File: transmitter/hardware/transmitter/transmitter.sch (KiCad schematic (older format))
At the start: 29 parts, among them J1 SOIL, J2 SOIL, J3 USB_UART, J4 PWR, J5 SOIL, J6 SOIL, J7 SOIL, J8 SOIL, SW1 SW_SPST, SW2 SW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

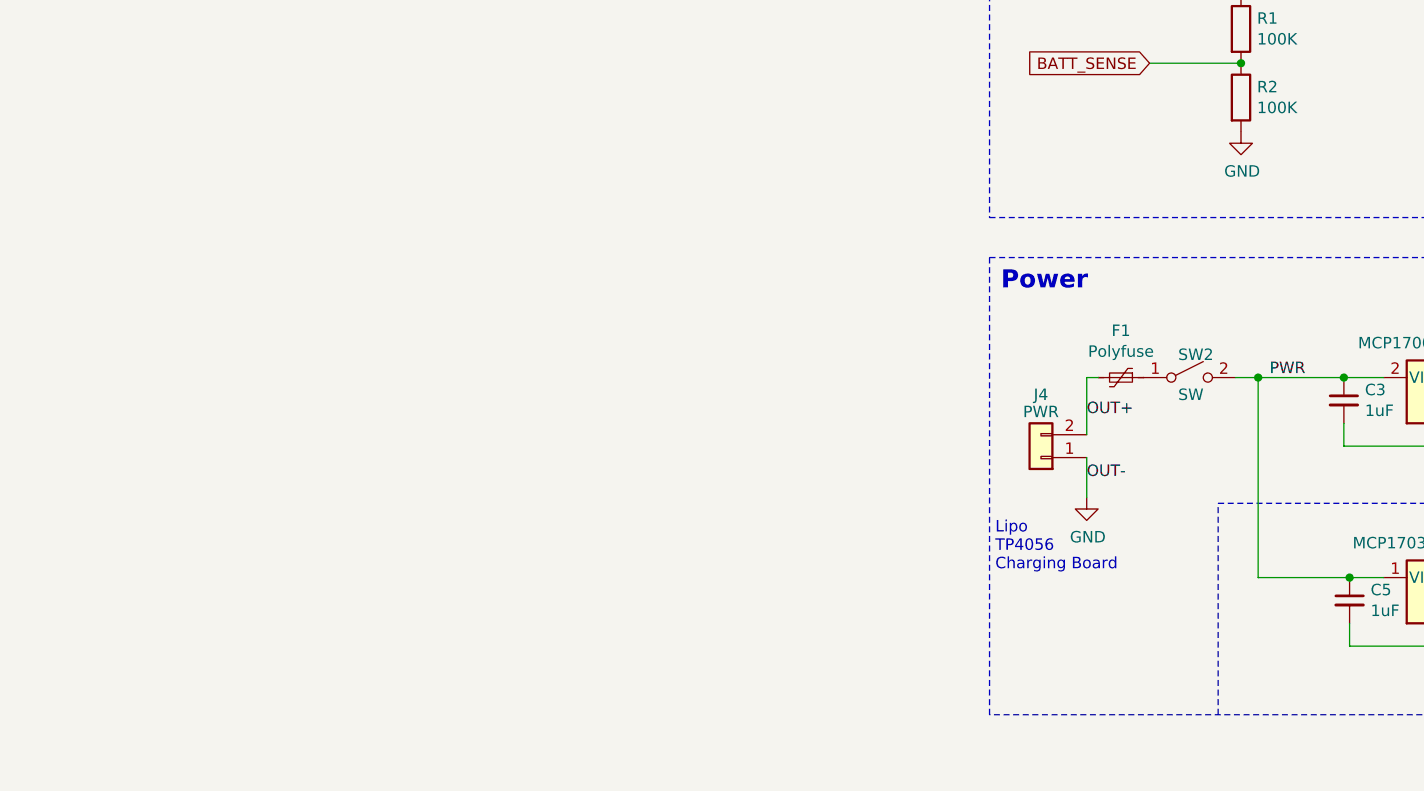
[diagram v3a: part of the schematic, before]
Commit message: Lower power turn off
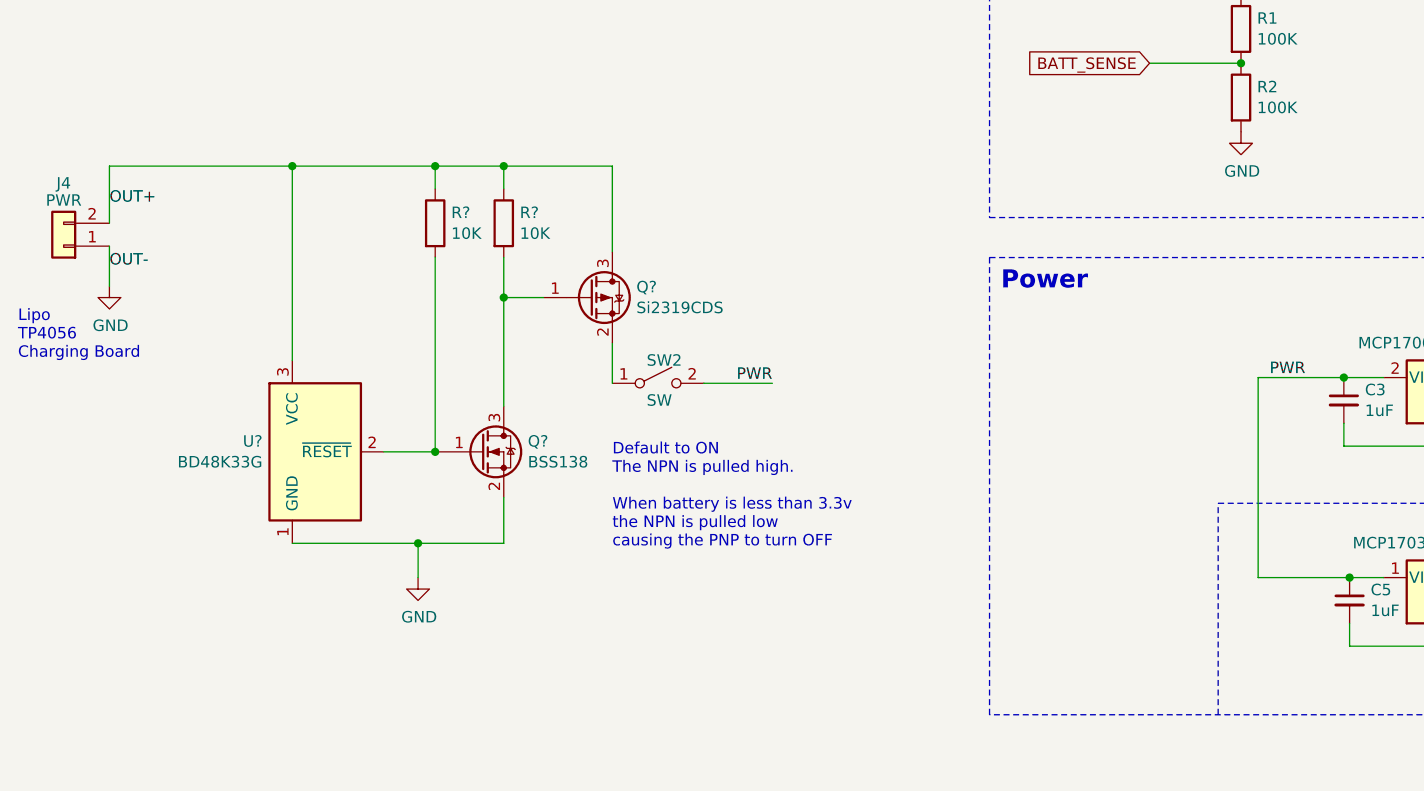
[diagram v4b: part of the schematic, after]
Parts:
- removed F1: Polyfuse, Fuse:Fuse_1812_4532Metric_Pad1.30x3.40mm_HandSolder, symbol Device:Polyfuse_Small
- added Q?: Si2319CDS, Package_TO_SOT_SMD:SOT-23, symbol Transistor_FET:Si2319CDS
- added Q?: BSS138, Package_TO_SOT_SMD:SOT-23, symbol Transistor_FET:BSS138
- added R? (x2): 10K, Resistor_SMD:R_0603_1608Metric_Pad1.05x0.95mm_HandSolder, symbol Device:R
- added U?: BD48K33G, symbol Power_Supervisor:TCM809
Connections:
- net GND: now also Q?.2 (S), U?.1 (GND)
- net OUT+: now also Q?.3 (D), R?.1, R?.1, U?.3 (VCC)
- net at SW2.1 (A): now also Q?.2 (S)
- new net: Q?.1 (G), Q?.3 (D), R?.2
- new net: Q?.1 (G), R?.2, U?.2 (~RESET~)
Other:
- note added: "Default to ON \nThe NPN is pulled high.\n\nWhen battery is less than 3.3v \nthe NPN is pulled low \ncausing the PNP to turn OFF"
- moved on the sheet: J4, SW2
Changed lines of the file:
@@
 	6025 4725 5825 4725
-$Comp
-L Device:Polyfuse_Small F1
-U 1 1 5DBEC73F
-P 1175 2600
-F 0 "F1" V 970 2600 50  0000 C CNN
-F 1 "Polyfuse" V 1061 2600 50  0000 C CNN
-F 2 "Fuse:Fuse_1812_4532Metric_Pad1.30x3.40mm_HandSolder" H 1225 2400 50  0001 L CNN
-F 3 "~" H 1175 2600 50  0001 C CNN
-	1    1175 2600
-	0    1    1    0
-$EndComp
 $Comp
 L Switch:SW_SPST SW2
 U 1 1 5DBF0754
-P 1475 2600
-F 0 "SW2" H 1425 2700 50  0000 L CNN
-F 1 "SW" H 1425 2525 50  0000 L CNN
-F 2 "Connector_PinHeader_2.54mm:PinHeader_1x02_P2.54mm_Vertical" H 1475 2600 50  0001 C CNN
-F 3 "" H 1475 2600 50  0001 C CNN
-	1    1475 2600
+P -850 2625
+F 0 "SW2" H -900 2725 50  0000 L CNN
+F 1 "SW" H -900 2550 50  0000 L CNN
+F 2 "Connector_PinHeader_2.54mm:PinHeader_1x02_P2.54mm_Vertical" H -850 2625 50  0001 C CNN
+F 3 "" H -850 2625 50  0001 C CNN
+	1    -850 2625
 	1    0    0    -1
 $EndComp
@@
 L Connector_Generic:Conn_01x02 J4
 U 1 1 5DBF418E
-P 825 2950
-F 0 "J4" H 825 2675 50  0000 C CNN
-F 1 "PWR" H 825 2750 50  0000 C CNN
-F 2 "tp4056:tp4056" H 825 2950 50  0001 C CNN
-F 3 "~" H 825 2950 50  0001 C CNN
-	1    825  2950
+P -3450 2025
+F 0 "J4" H -3450 1750 50  0000 C CNN
+F 1 "PWR" H -3450 1825 50  0000 C CNN
+F 2 "tp4056:tp4056" H -3450 2025 50  0001 C CNN
+F 3 "~" H -3450 2025 50  0001 C CNN
+	1    -3450 2025
 	-1   0    0    1
 $EndComp
-Text Notes 625  3450 0    50   ~ 0
+Text Notes -3650 2525 0    50   ~ 0
 Lipo \nTP4056\nCharging Board
 Wire Wire Line
-	1075 2600 1025 2600
-Wire Wire Line
-	1025 2600 1025 2850
-Wire Wire Line
-	1025 2950 1025 3125
-Text Label 1025 2775 0    50   ~ 0
+	-3250 1675 -3250 1925
+Wire Wire Line
+	-3250 2025 -3250 2200
+Text Label -3250 1850 0    50   ~ 0
 OUT+
-Text Label 1025 3050 0    50   ~ 0
+Text Label -3250 2125 0    50   ~ 0
 OUT-
 $Comp
@@
 L power:GND #PWR015
 U 1 1 5DC1E5D1
-P 1025 3125
-F 0 "#PWR015" H 1025 2875 50  0001 C CNN
-F 1 "GND" H 1030 2952 50  0000 C CNN
-F 2 "" H 1025 3125 50  0001 C CNN
-F 3 "" H 1025 3125 50  0001 C CNN
-	1    1025 3125
+P -3250 2200
+F 0 "#PWR015" H -3250 1950 50  0001 C CNN
+F 1 "GND" H -3245 2027 50  0000 C CNN
+F 2 "" H -3250 2200 50  0001 C CNN
+F 3 "" H -3250 2200 50  0001 C CNN
+	1    -3250 2200
 	1    0    0    -1
 $EndComp
@@
 Wire Wire Line
 	2150 2600 2325 2600
-Wire Wire Line
-	1675 2600 1775 2600
 Wire Wire Line
 	3000 2600 3350 2600
@@
 Wire Wire Line
 	1775 3475 2175 3475
-Connection ~ 1775 2600
 Wire Wire Line
 	1775 2600 2150 2600
@@
 Wire Notes Line
 	3775 3150 3775 4075
+$Comp
+L Transistor_FET:Si2319CDS Q?
+U 1 1 5E0DACCE
+P -1150 2250
+F 0 "Q?" H -945 2296 50  0000 L CNN
+F 1 "Si2319CDS" H -945 2205 50  0000 L CNN
+F 2 "Package_TO_SOT_SMD:SOT-23" H -950 2175 50  0001 L CIN
+F 3 "http://www.vishay.com/docs/66709/si2319cd.pdf" H -1150 2250 50  0001 L CNN
+	1    -1150 2250
+	1    0    0    -1
+$EndComp
+$Comp
+L Device:R R?
+U 1 1 5E0DDFAF
+P -1525 1925
+F 0 "R?" H -1455 1971 50  0000 L CNN
+F 1 "10K" H -1455 1880 50  0000 L CNN
+F 2 "Resistor_SMD:R_0603_1608Metric_Pad1.05x0.95mm_HandSolder" V -1595 1925 50  0001 C CNN
+F 3 "~" H -1525 1925 50  0001 C CNN
+	1    -1525 1925
+	1    0    0    -1
+$EndComp
+Wire Wire Line
+	-1525 2075 -1525 2250
+Wire Wire Line
+	-1525 2250 -1350 2250
+Wire Wire Line
+	-1050 2050 -1050 1675
+Wire Wire Line
+	-1050 1675 -1525 1675
+Connection ~ -1525 1675
+Wire Wire Line
+	-1525 1675 -1525 1775
+Text Notes -1050 3350 0    50   ~ 0
+Default to ON \nThe NPN is pulled high.\n\nWhen battery is less than 3.3v \nthe NPN is pulled low \ncausing the PNP to turn OFF
+$Comp
+L Transistor_FET:BSS138 Q?
+U 1 1 5E0E3313
+P -1625 2925
+F 0 "Q?" H -1420 2971 50  0000 L CNN
+F 1 "BSS138" H -1420 2880 50  0000 L CNN
+F 2 "Package_TO_SOT_SMD:SOT-23" H -1425 2850 50  0001 L CIN
+F 3 "https://www.fairchildsemi.com/datasheets/BS/BSS138.pdf" H -1625 2925 50  0001 L CNN
+	1    -1625 2925
+	1    0    0    -1
+$EndComp
+Wire Wire Line
+	-1525 2250 -1525 2725
+Connection ~ -1525 2250
+$Comp
+L power:GND #PWR?
+U 1 1 5E0E512F
+P -1900 3475
+F 0 "#PWR?" H -1900 3225 50  0001 C CNN
+F 1 "GND" H -1895 3302 50  0000 C CNN
+F 2 "" H -1900 3475 50  0001 C CNN
+F 3 "" H -1900 3475 50  0001 C CNN
+	1    -1900 3475
+	1    0    0    -1
+$EndComp
+$Comp
+L Device:R R?
+U 1 1 5E0E705E
+P -1825 1925
+F 0 "R?" H -1755 1971 50  0000 L CNN
+F 1 "10K" H -1755 1880 50  0000 L CNN
+F 2 "Resistor_SMD:R_0603_1608Metric_Pad1.05x0.95mm_HandSolder" V -1895 1925 50  0001 C CNN
+F 3 "~" H -1825 1925 50  0001 C CNN
+	1    -1825 1925
+	1    0    0    -1
+$EndComp
+Wire Wire Line
+	-1825 2075 -1825 2925
+Wire Wire Line
+	-1825 1775 -1825 1675
+Wire Wire Line
+	-1825 1675 -1525 1675
+Connection ~ -1825 1675
+Wire Wire Line
+	-1050 2450 -1050 2625
+Wire Wire Line
+	-650 2625 -350 2625
+Text Label -350 2625 2    50   ~ 0
+PWR
+$Comp
+L Power_Supervisor:TCM809 U?
+U 1 1 5E0F3C0E
+P -2350 2925
+F 0 "U?" H -2580 2971 50  0000 R CNN
+F 1 "BD48K33G" H -2580 2880 50  0000 R CNN
+F 2 "" H -2750 3075 50  0001 C CNN
+F 3 "http://ww1.microchip.com/downloads/en/DeviceDoc/21661E.pdf" H -2650 3175 50  0001 C CNN
+	1    -2350 2925
+	1    0    0    -1
+$EndComp
+Wire Wire Line
+	-3250 1675 -2450 1675
+Wire Wire Line
+	-2050 2925 -1825 2925
+Connection ~ -1825 2925
+Wire Wire Line
+	-2450 3325 -1900 3325
+Wire Wire Line
+	-1900 3325 -1900 3475
+Wire Wire Line
+	-1525 3325 -1900 3325
+Connection ~ -1900 3325
+Wire Wire Line
+	-1525 3125 -1525 3325
+Wire Wire Line
+	-2450 2525 -2450 1675
+Connection ~ -2450 1675
+Wire Wire Line
+	-2450 1675 -1825 1675
 $EndSCHEMATC

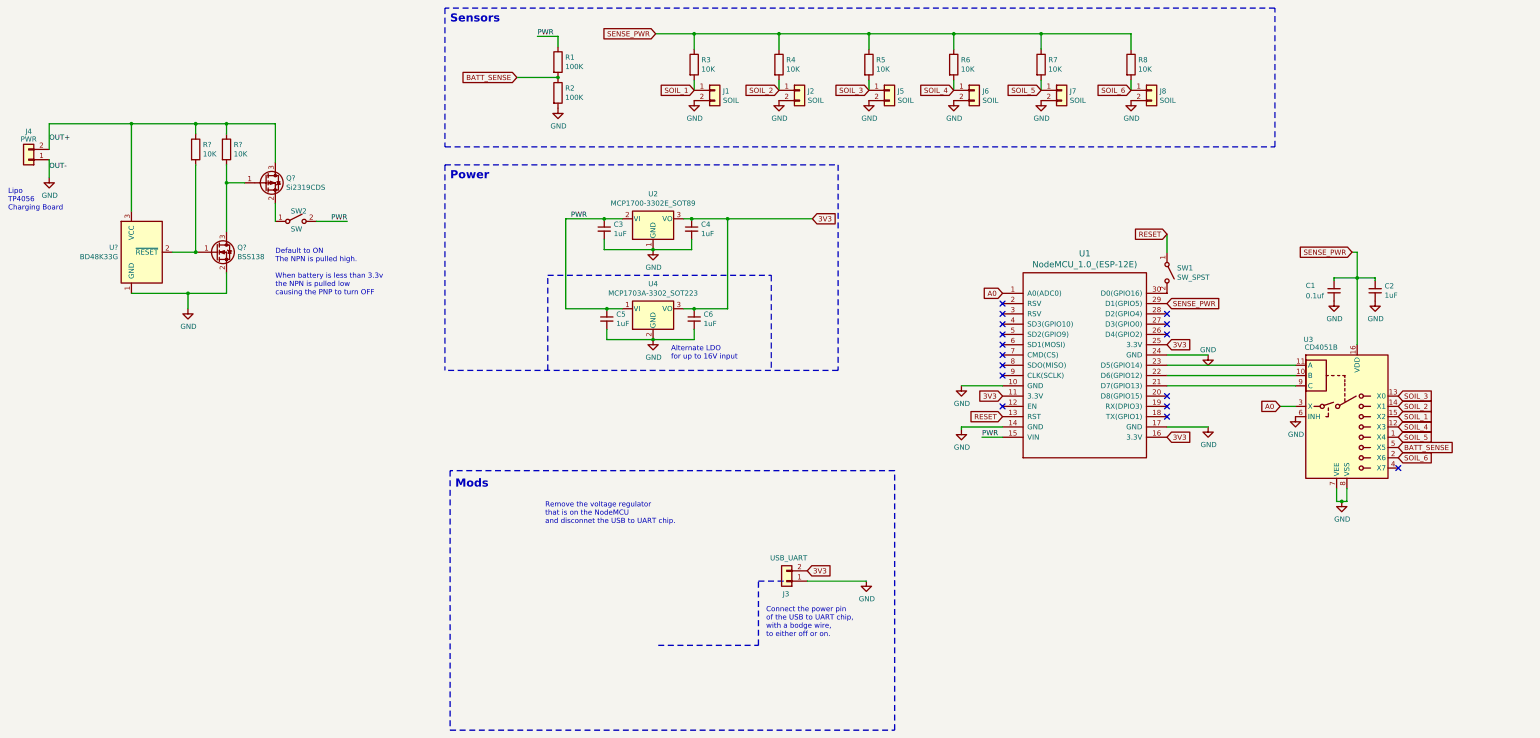
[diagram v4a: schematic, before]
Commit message: External low power timer
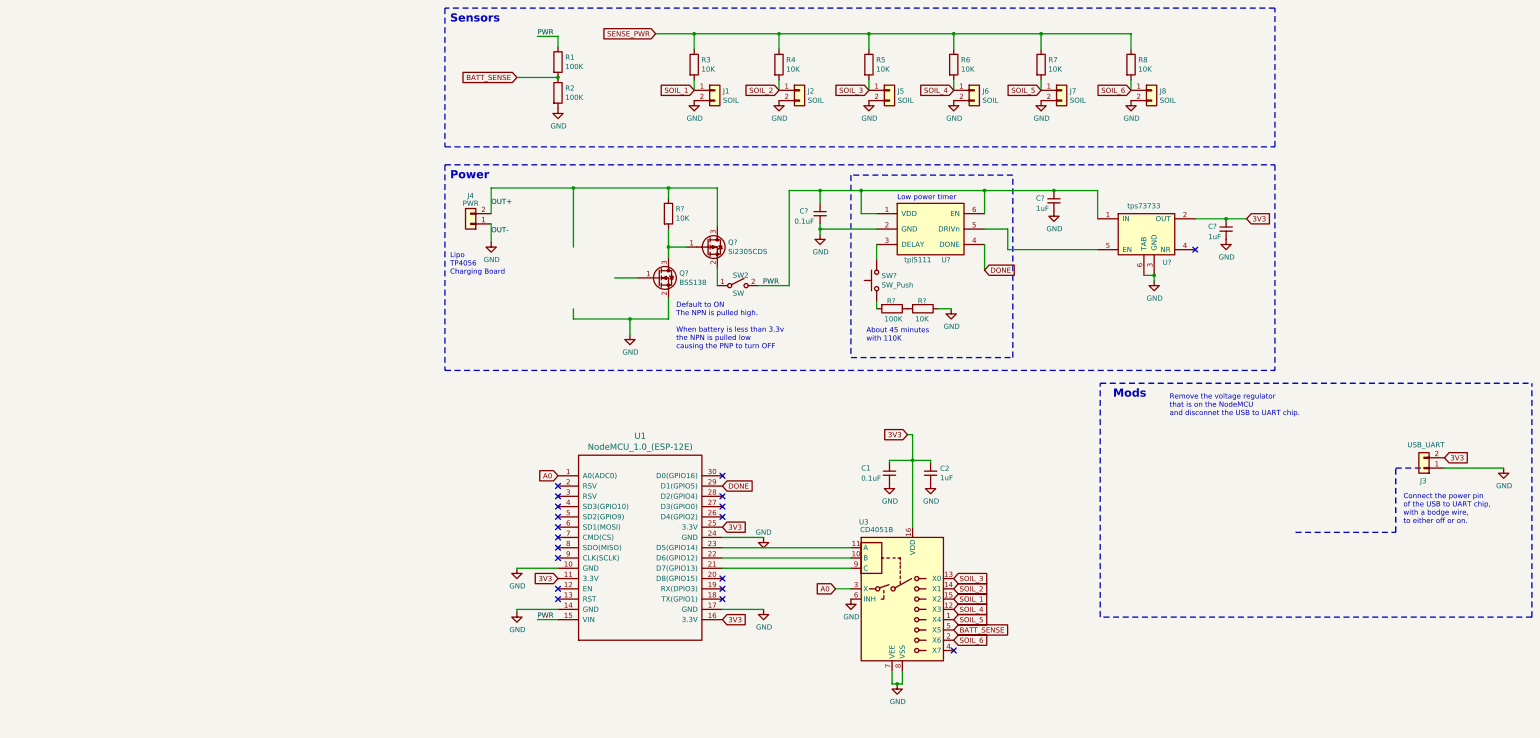
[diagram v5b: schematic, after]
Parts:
- removed C3, C4, C5, C6: 1uF, Capacitor_SMD:C_0603_1608Metric_Pad1.05x0.95mm_HandSolder, symbol Device:C_Small
- removed R?: 10K, Resistor_SMD:R_0603_1608Metric_Pad1.05x0.95mm_HandSolder, symbol Device:R
- removed SW1: SW_SPST, Connector_PinHeader_2.54mm:PinHeader_1x02_P2.54mm_Vertical, symbol Switch:SW_SPST
- removed U2: MCP1700-3302E_SOT89, Package_TO_SOT_SMD:SOT-89-3, symbol Regulator_Linear:MCP1700-3302E_SOT89
- removed U4: MCP1703A-3302_SOT223, Package_TO_SOT_SMD:SOT-223-3_TabPin2, symbol Regulator_Linear:MCP1703A-3302_SOT223
- removed U?: BD48K33G, symbol Power_Supervisor:TCM809
- added C?: 0.1uF, symbol Device:C_Small
- added C? (x2): 1uF, Capacitor_SMD:C_0603_1608Metric_Pad1.05x0.95mm_HandSolder, symbol Device:C_Small
- added R?: 100K, Resistor_SMD:R_0603_1608Metric_Pad1.05x0.95mm_HandSolder, symbol Device:R
- added R?: 10K, Resistor_SMD:R_0603_1608Metric_Pad1.05x0.95mm_HandSolder, symbol Device:R
- added SW?: SW_Push, symbol Switch:SW_Push
- added U?: tps73733, symbol tps737:tps73733
- added U?: tpl5111, symbol tpl5111:tpl5111
- C1: value 0.1uf -> 0.1uF
- Q?: value Si2319CDS -> Si2305CDS
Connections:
- net labels added: DONE
- net labels removed: RESET
- wire segments 84 -> 87
- no-connect marks 16 -> 19
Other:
- note added: "About 45 minutes \nwith 110K"
- note added: "Low power timer"
- note removed: "Alternate LDO\nfor up to 16V input"
- moved on the sheet: C1, C2, J3, J4, Q?, R?, SW2, U1, U3

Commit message: Low power
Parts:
- added C6: 1uF, Capacitor_SMD:C_0603_1608Metric_Pad1.05x0.95mm_HandSolder, symbol Device:C_Small
- added C7: 1000pF, Capacitor_SMD:C_0603_1608Metric_Pad1.05x0.95mm_HandSolder, symbol Device:C_Small
- added Q1: Si2305CDS, Package_TO_SOT_SMD:SOT-23, symbol Transistor_FET:Si2319CDS
- added Q2: BSS138, Package_TO_SOT_SMD:SOT-23, symbol Transistor_FET:BSS138
- added R10, R11, R9: 10K, Resistor_SMD:R_0603_1608Metric_Pad1.05x0.95mm_HandSolder, symbol Device:R
- added U5: BD4833G, symbol bd48x:BD4833G
- gave numbers to parts that had none: 11
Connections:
- net labels added: VBAT
- net labels removed: PWR, SENSE_PWR
- wire segments 87 -> 106
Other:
- note added: "Lipo \nTP4056\nCharging\nBoard"
- note added: "Under 3V3 cuttoff"
- note removed: "Lipo \nTP4056\nCharging Board"
- moved on the sheet: C3, C4, J1, J2, J5, J6, J7, J8, Q3, Q4, R1, R12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
